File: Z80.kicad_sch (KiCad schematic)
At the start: 7 parts, among them J13 Conn_02x06_Odd_Even, J14 Conn_02x20_Odd_Even, U4 Z80CPU

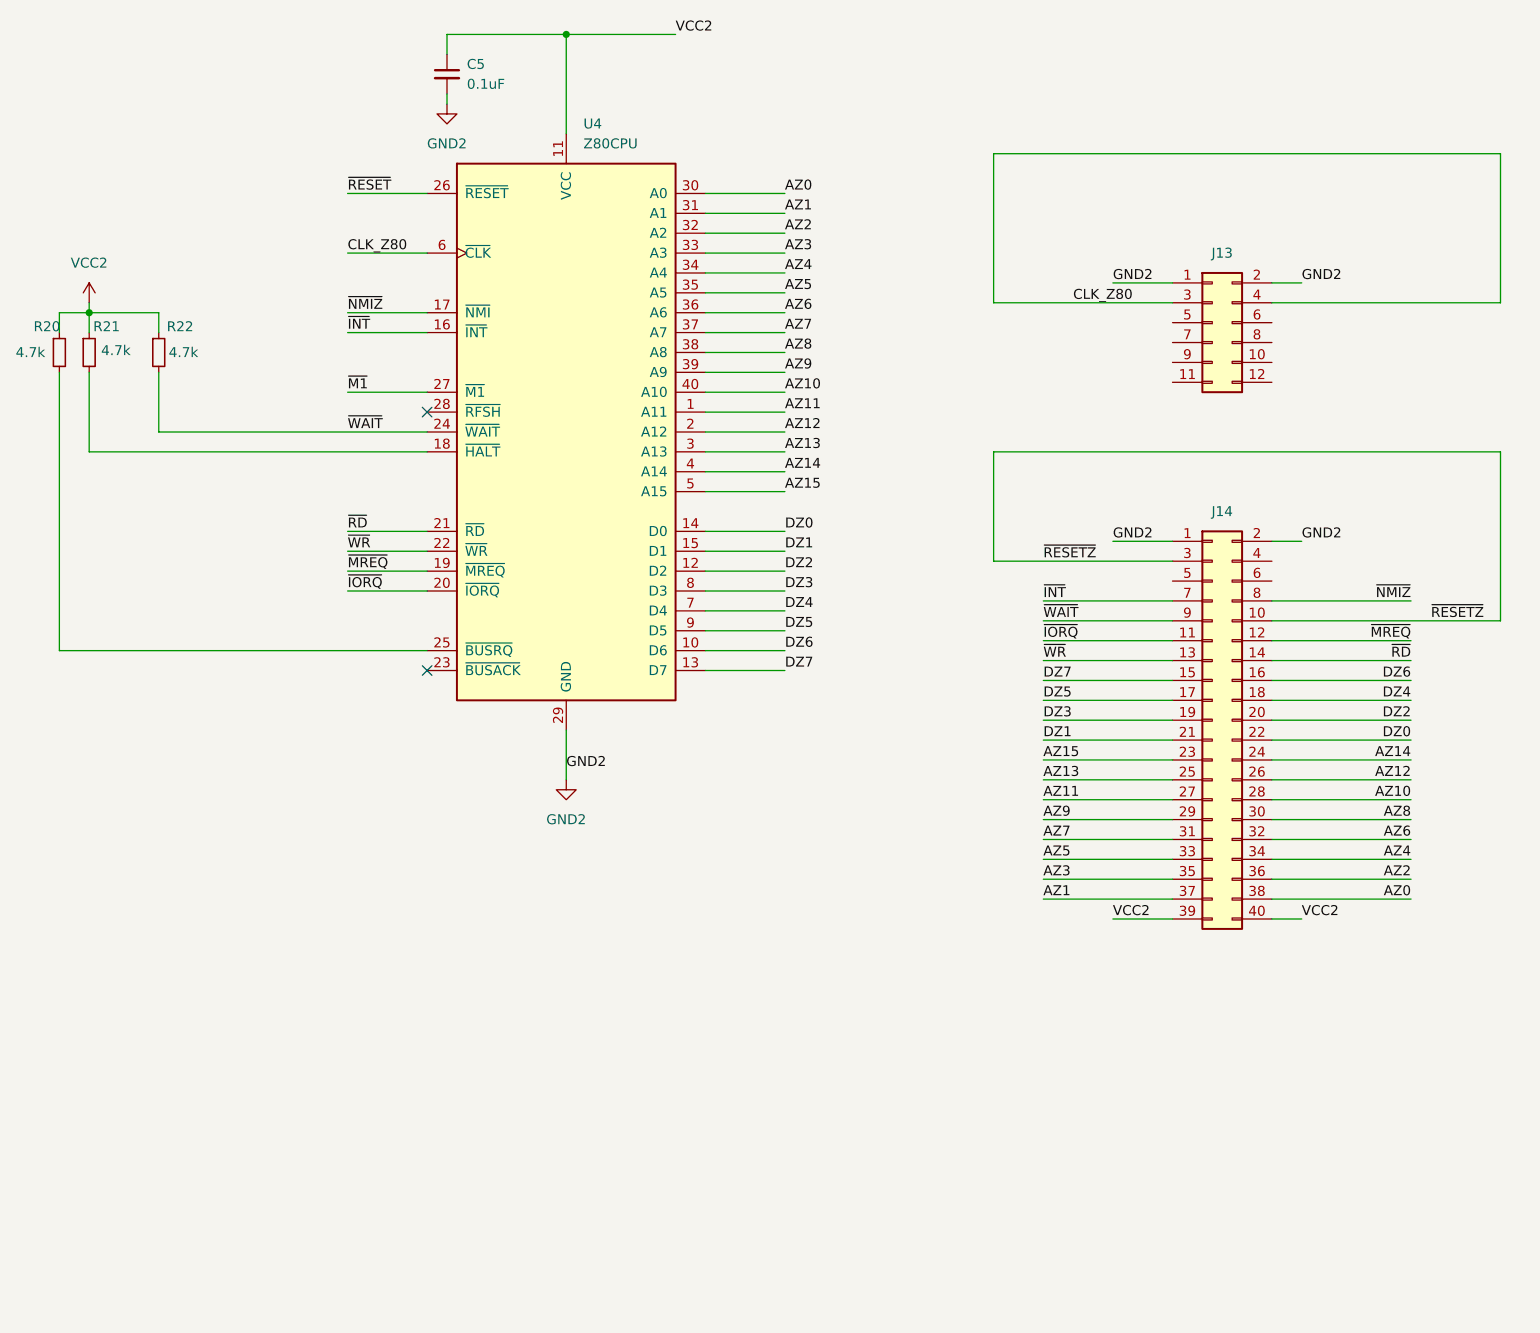
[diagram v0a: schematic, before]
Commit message: Update Z80.kicad_sch
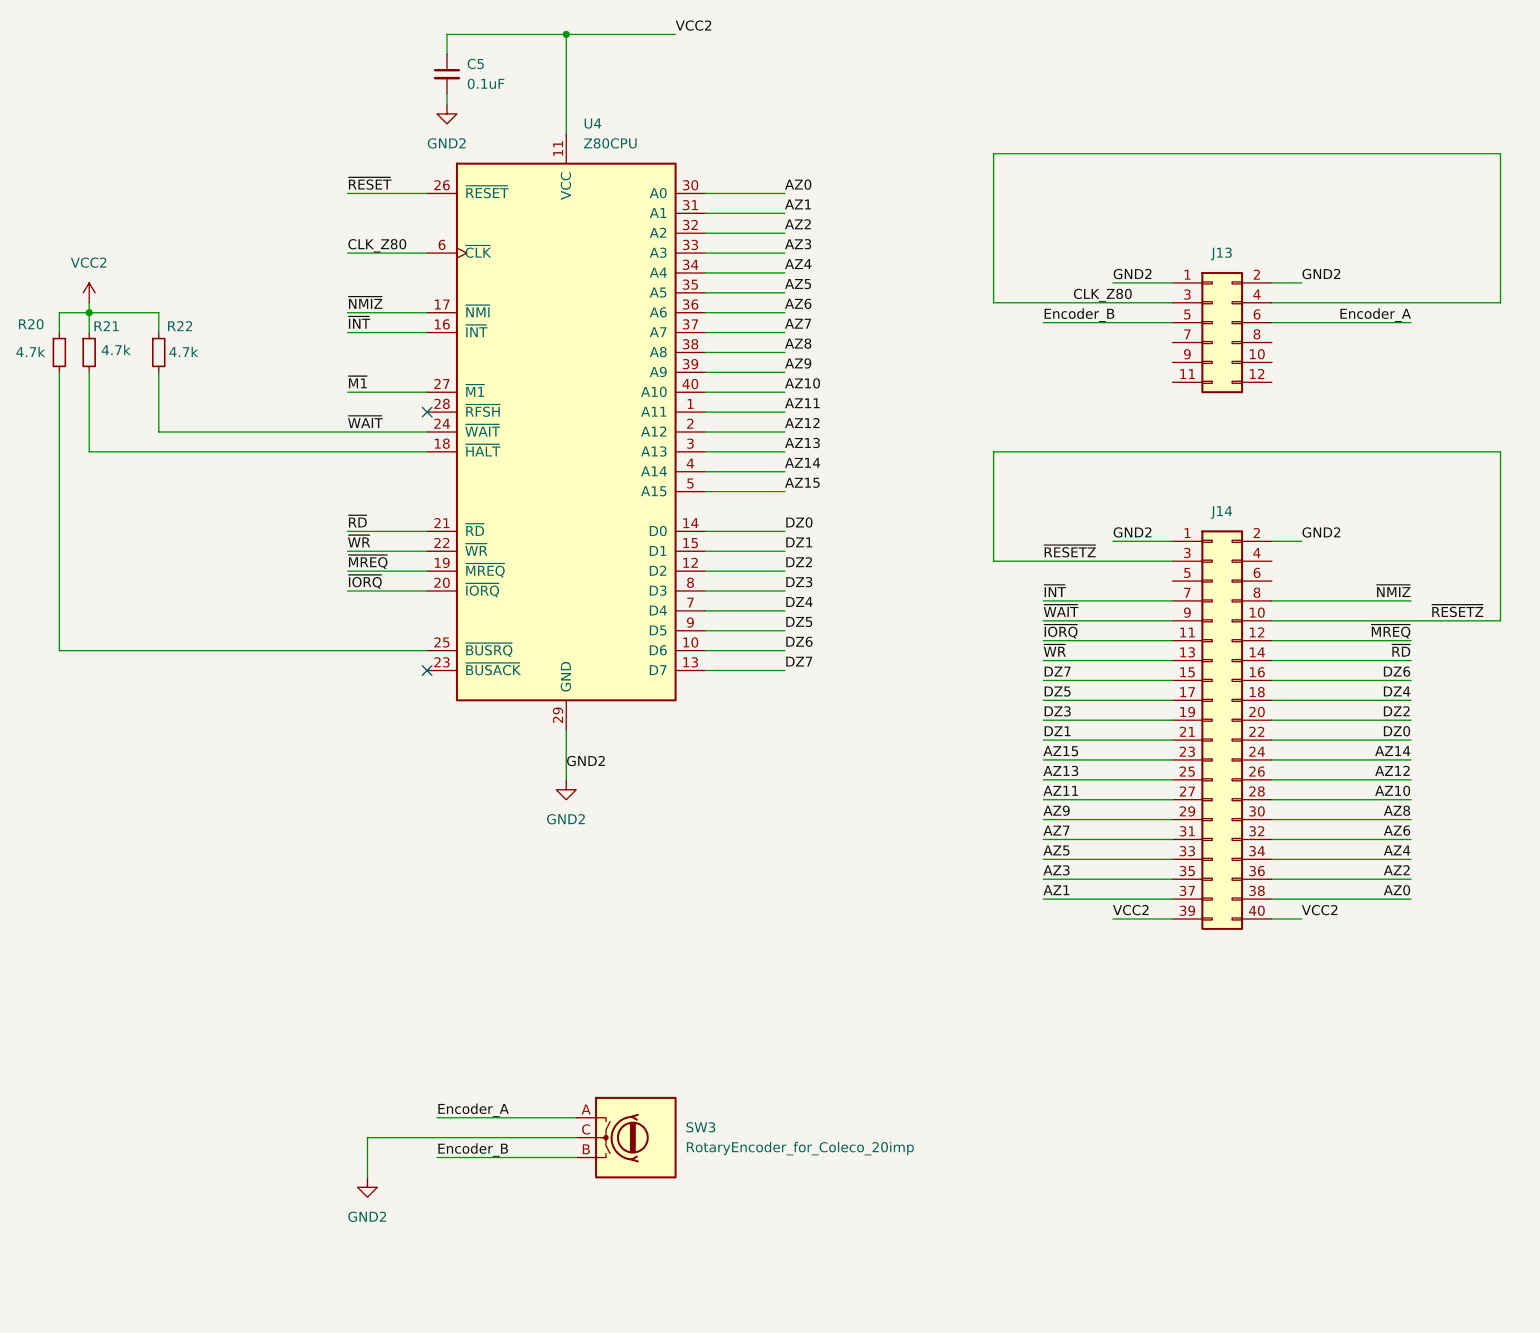
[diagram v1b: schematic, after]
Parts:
- added SW3: RotaryEncoder_for_Coleco_20imp, symbol Device:RotaryEncoder
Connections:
- net GND2: now also SW3.C
- net Encoder_B: now reaches J13.5 (Pin_5)
- net Encoder_B: now also SW3.B
- net Encoder_A: now reaches J13.6 (Pin_6)
- net Encoder_A: now also SW3.A
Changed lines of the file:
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@@
+	(wire
+		(pts
+			(xy 78.74 173.99) (xy 78.74 179.07)
+		)
+		(stroke
+			(width 0)
+			(type default)
+		)
+	)
 	(wire
 		(pts
@@
 	(wire
 		(pts
+			(xy 87.63 176.53) (xy 105.41 176.53)
+		)
+		(stroke
+			(width 0)
+			(type default)
+		)
+	)
+	(wire
+		(pts
 			(xy 194.31 123.19) (xy 212.09 123.19)
 		)
@@
 	(wire
 		(pts
+			(xy 212.09 69.85) (xy 194.31 69.85)
+		)
+		(stroke
+			(width 0)
+			(type default)
+		)
+	)
+	(wire
+		(pts
 			(xy 223.52 86.36) (xy 158.75 86.36)
 		)
@@
 	(wire
 		(pts
+			(xy 78.74 173.99) (xy 105.41 173.99)
+		)
+		(stroke
+			(width 0)
+			(type default)
+		)
+	)
+	(wire
+		(pts
 			(xy 88.9 40.64) (xy 88.9 41.91)
 		)
@@
 	(wire
 		(pts
+			(xy 165.1 69.85) (xy 181.61 69.85)
+		)
+		(stroke
+			(width 0)
+			(type default)
+		)
+	)
+	(wire
+		(pts
 			(xy 86.36 86.36) (xy 43.18 86.36)
 		)
@@
 		(pts
 			(xy 76.2 104.14) (xy 86.36 104.14)
+		)
+		(stroke
+			(width 0)
+			(type default)
+		)
+	)
+	(wire
+		(pts
+			(xy 87.63 171.45) (xy 105.41 171.45)
 		)
 		(stroke
@@
 		)
 	)
+	(label "Encoder_B"
+		(at 87.63 176.53 0)
+		(fields_autoplaced yes)
+		(effects
+			(font
+				(size 1.27 1.27)
+			)
+			(justify left bottom)
+		)
+	)
 	(label "DZ4"
 		(at 132.08 106.68 0)
@@
 		)
 	)
+	(label "Encoder_A"
+		(at 212.09 69.85 180)
+		(fields_autoplaced yes)
+		(effects
+			(font
+				(size 1.27 1.27)
+			)
+			(justify right bottom)
+		)
+	)
 	(label "GND2"
 		(at 104.14 127 0)
@@
 		)
 	)
+	(label "Encoder_B"
+		(at 165.1 69.85 0)
+		(fields_autoplaced yes)
+		(effects
+			(font
+				(size 1.27 1.27)
+			)
+			(justify left bottom)
+		)
+	)
 	(label "DZ2"
 		(at 132.08 101.6 0)
@@
 			)
 			(justify right bottom)
+		)
+	)
+	(label "Encoder_A"
+		(at 87.63 171.45 0)
+		(fields_autoplaced yes)
+		(effects
+			(font
+				(size 1.27 1.27)
+			)
+			(justify left bottom)
 		)
 	)
@@
 	(symbol
 		(lib_id "power:GND")
+		(at 78.74 179.07 0)
+		(unit 1)
+		(exclude_from_sim no)
+		(in_bom yes)
+		(on_board yes)
+		(dnp no)
+		(fields_autoplaced yes)
+		(property "Reference" "#PWR019"
+			(at 78.74 185.42 0)
+			(effects
+				(font
+					(size 1.27 1.27)
+				)
+				(hide yes)
+			)
+		)
+		(property "Value" "GND2"
+			(at 78.74 184.15 0)
+			(effects
+				(font
+					(size 1.27 1.27)
+				)
+			)
+		)
+		(property "Footprint" ""
+			(at 78.74 179.07 0)
+			(effects
+				(font
+					(size 1.27 1.27)
+				)
+				(hide yes)
+			)
+		)
+		(property "Datasheet" ""
+			(at 78.74 179.07 0)
+			(effects
+				(font
+					(size 1.27 1.27)
+				)
+				(hide yes)
+			)
+		)
+		(property "Description" "Power symbol creates a global label with name \"GND\" , ground"
+			(at 78.74 179.07 0)
+			(effects
+				(font
+					(size 1.27 1.27)
+				)
+				(hide yes)
+			)
+		)
+		(pin "1"
+		)
+		(instances
+			(project "RP2350B_Consol"
+				(path "/6e8f208f-ca10-4f24-b31c-14a8c528e849/e3ce755a-b3ff-4652-8810-baffe7a99d3c"
+					(reference "#PWR019")
+					(unit 1)
+				)
+			)
+		)
+	)
+	(symbol
+		(lib_id "power:GND")
 		(at 88.9 41.91 0)
 		(unit 1)
@@
 				(path "/6e8f208f-ca10-4f24-b31c-14a8c528e849/e3ce755a-b3ff-4652-8810-baffe7a99d3c"
 					(reference "#PWR017")
+					(unit 1)
+				)
+			)
+		)
+	)
+	(symbol
+		(lib_id "Device:RotaryEncoder")
+		(at 113.03 173.99 0)
+		(unit 1)
+		(exclude_from_sim no)
+		(in_bom yes)
+		(on_board yes)
+		(dnp no)
+		(fields_autoplaced yes)
+		(property "Reference" "SW3"
+			(at 119.38 172.7199 0)
+			(effects
+				(font
+					(size 1.27 1.27)
+				)
+				(justify left)
+			)
+		)
+		(property "Value" "RotaryEncoder_for_Coleco_20imp"
+			(at 119.38 175.2599 0)
+			(effects
+				(font
+					(size 1.27 1.27)
+				)
+				(justify left)
+			)
+		)
+		(property "Footprint" ""
+			(at 109.22 169.926 0)
+			(effects
+				(font
+					(size 1.27 1.27)
+				)
+				(hide yes)
+			)
+		)
+		(property "Datasheet" "~"
+			(at 113.03 167.386 0)
+			(effects
+				(font
+					(size 1.27 1.27)
+				)
+				(hide yes)
+			)
+		)
+		(property "Description" "Rotary encoder, dual channel, incremental quadrate outputs"
+			(at 113.03 173.99 0)
+			(effects
+				(font
+					(size 1.27 1.27)
+				)
+				(hide yes)
+			)
+		)
+		(pin "B"
+		)
+		(pin "A"
+		)
+		(pin "C"
+		)
+		(instances
+			(project "RP2350B_Consol"
+				(path "/6e8f208f-ca10-4f24-b31c-14a8c528e849/e3ce755a-b3ff-4652-8810-baffe7a99d3c"
+					(reference "SW3")
 					(unit 1)
 				)
@@
 		(dnp no)
 		(property "Reference" "R20"
-			(at 36.068 70.358 0)
-			(effects
-				(font
+			(at 34.036 70.104 0)
+			(effects
+				(font

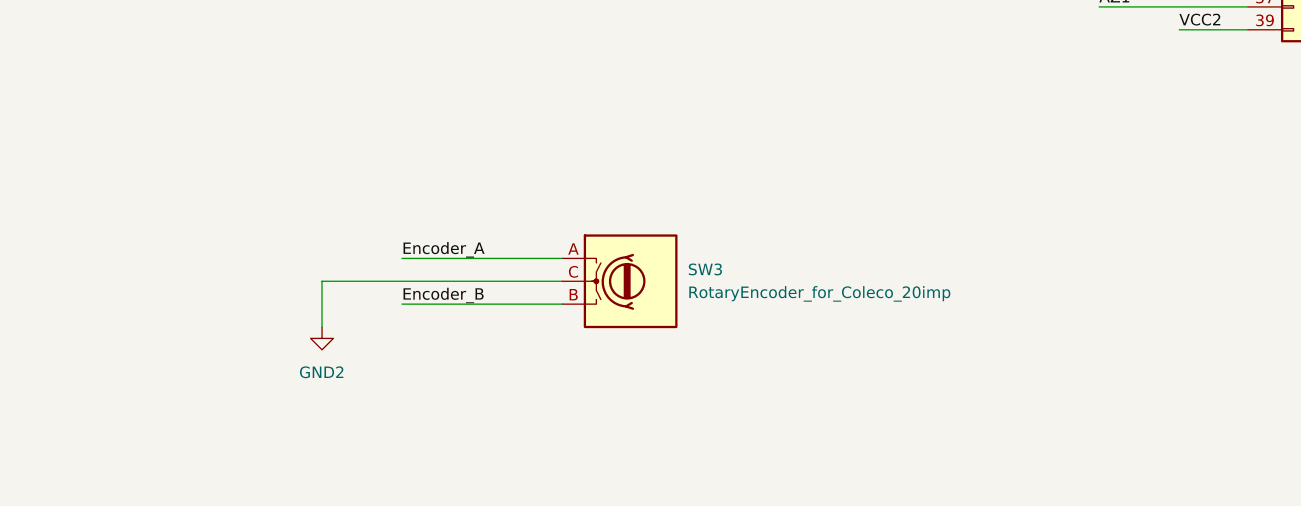
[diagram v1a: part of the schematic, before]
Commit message: Update Z80.kicad_sch
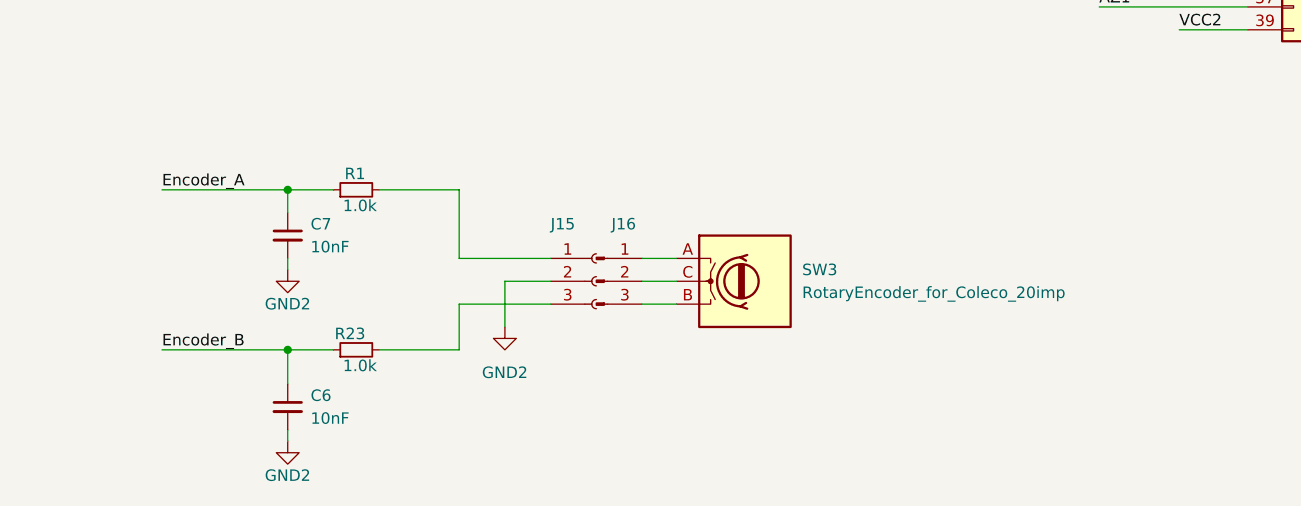
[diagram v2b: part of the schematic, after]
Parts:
- added C6, C7: 10nF, Capacitor_SMD:C_0805_2012Metric_Pad1.18x1.45mm_HandSolder, symbol Device:C_Small
- added J15: Conn_01x03_Socket, symbol Connector:Conn_01x03_Socket
- added J16: Conn_01x03_Pin, symbol Connector:Conn_01x03_Pin
- added R1, R23: 1.0k, Resistor_SMD:R_0805_2012Metric_Pad1.20x1.40mm_HandSolder, symbol Device:R_Small
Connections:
- net Encoder_A: now also C7.1, R1.1; no longer SW3.A
- net Encoder_B: now also C6.1, R23.1; no longer SW3.B
- net GND2: now also C6.2, C7.2, J15.2 (Pin_2); no longer SW3.C
- new net: J15.3 (Pin_3), R23.2
- new net: J16.1 (Pin_1), SW3.A
- new net: J16.2 (Pin_2), SW3.C
- new net: J16.3 (Pin_3), SW3.B
- new net: J15.1 (Pin_1), R1.2
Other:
- moved on the sheet: SW3
